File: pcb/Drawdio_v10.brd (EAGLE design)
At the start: 82.1 x 14.1 mm, 15 parts, among them IC1 TLC551, Q1 BC327

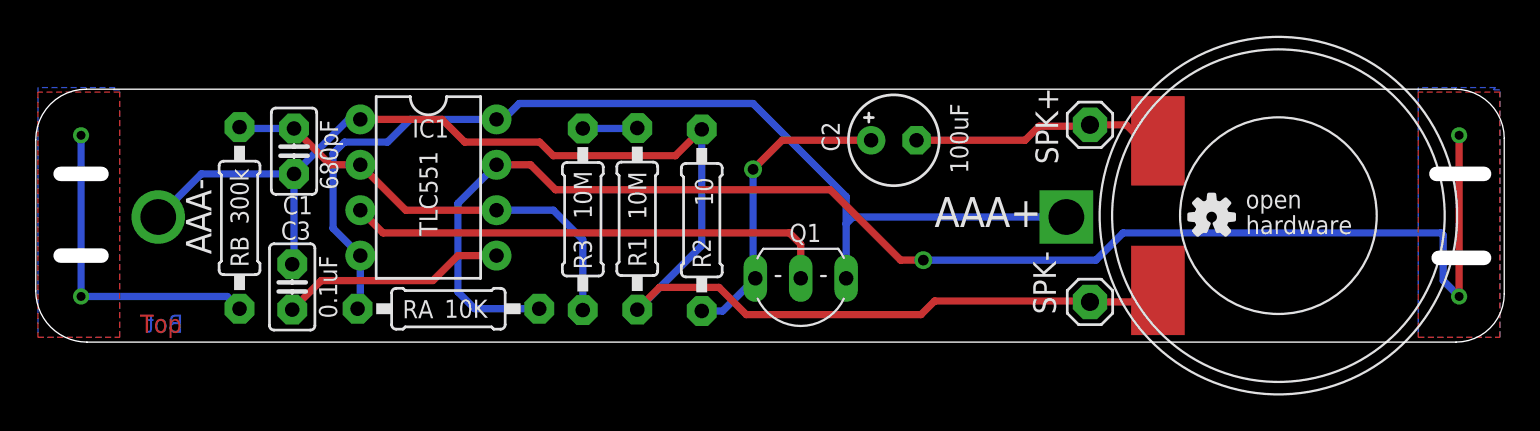
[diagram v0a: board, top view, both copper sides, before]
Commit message: updated schematics
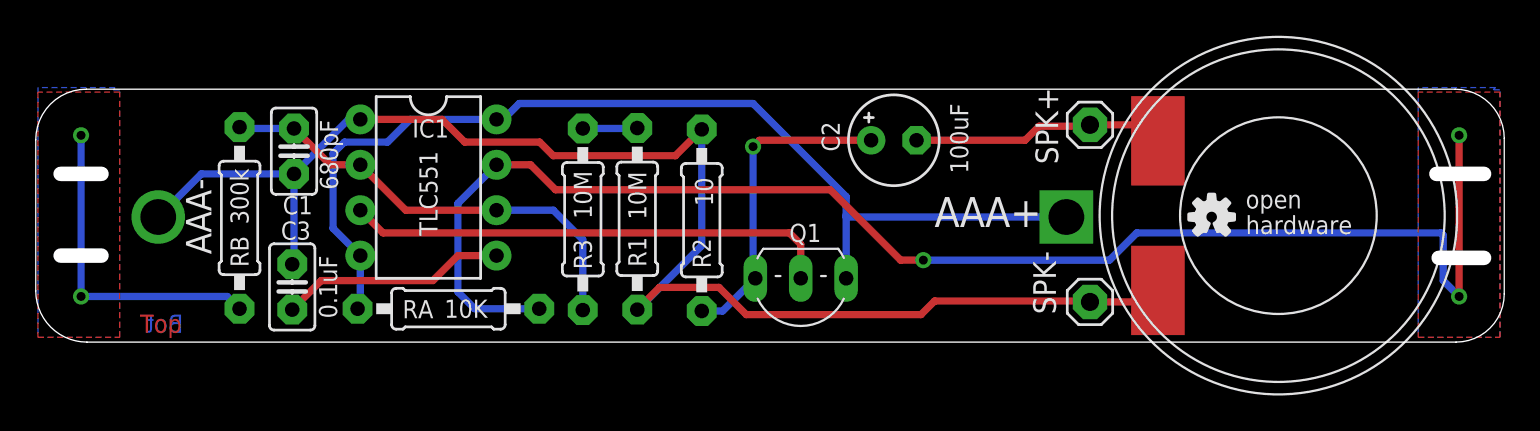
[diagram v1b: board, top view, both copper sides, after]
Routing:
- net N$3: track 17.2 -> 17.9 mm
